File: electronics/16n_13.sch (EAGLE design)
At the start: 112 parts, among them J1 PJ302M, J10 PJ302M, J11 PJ302M, J12 PJ302M, J13 PJ302M, J14 PJ302M, J15 PJ302M, J16 PJ302M, J2 PJ302M, J3 PJ302M, J4 PJ302M, J5 PJ302M, J6 PJ302M, J7 PJ302M, J8 PJ302M, J9 PJ302M, U1 MCP6004_SMD, U2 MCP6004_SMD, U3 MCP6004_SMD, U4 MCP6004_SMD, U5 MCP6004_SMD, U6 MCP6004_SMD, U7 MCP6004_SMD, U8 MCP6004_SMD, U9 CD74HC4067SM96

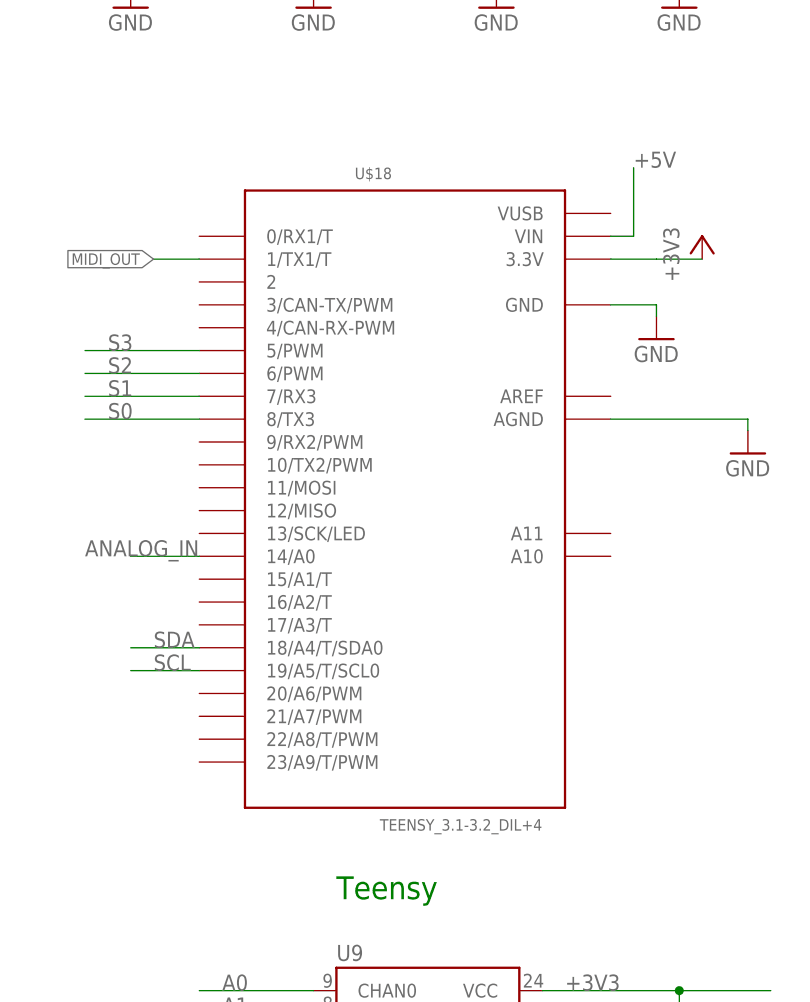
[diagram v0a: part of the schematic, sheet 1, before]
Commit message: Given Teensy 3.2 AREF is 3.3V... let's strip out the inner pins.
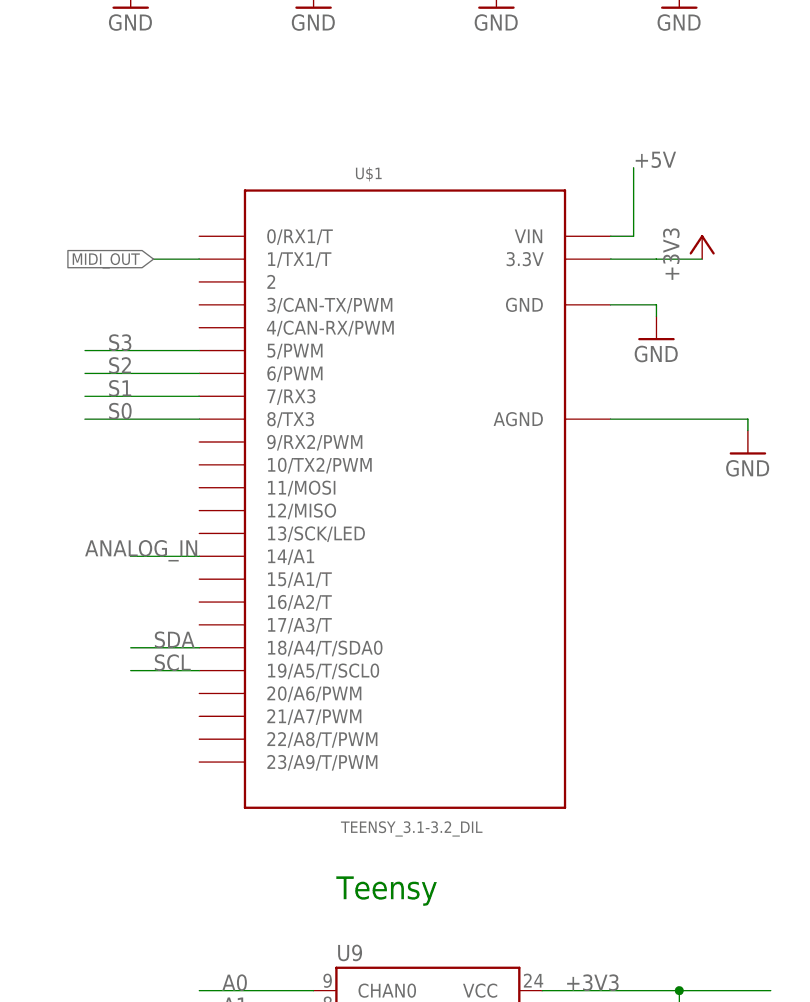
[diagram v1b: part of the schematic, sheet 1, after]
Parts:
- removed U$18: TEENSY_3.1-3.2_DIL+4, Teensy_3_and_LC_Series_Boards_v1.4:TEENSY_3.1-3.2_DIL+4
- added U$1: TEENSY_3.1-3.2_DIL, Teensy_3_and_LC_Series_Boards_v1.4:TEENSY_3.1-3.2_DIL
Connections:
- net +3V3: now also U$1.3.3V; no longer U$18.3.3V
- net +5V: now also U$1.VIN; no longer U$18.VIN
- net ANALOG_IN: now also U$1.14/A1; no longer U$18.14/A0
- net GND: now also U$1.AGND, U$1.GND; no longer U$18.AGND, U$18.GND
- net MIDI_OUT: now also U$1.1/TX1/T; no longer U$18.1/TX1/T
- net S0: now also U$1.8/TX3; no longer U$18.8/TX3
- net S1: now also U$1.7/RX3; no longer U$18.7/RX3
- net S2: now also U$1.6/PWM; no longer U$18.6/PWM
- net S3: now also U$1.5/PWM; no longer U$18.5/PWM
- net SCL: now also U$1.19/A5/T/SCL0; no longer U$18.19/A5/T/SCL0
- net SDA: now also U$1.18/A4/T/SDA0; no longer U$18.18/A4/T/SDA0
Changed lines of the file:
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@@
 <part name="GND24" library="supply1" deviceset="GND" device=""/>
 <part name="C9" library="rcl" library_urn="urn:adsk.eagle:library:334" deviceset="C-EU" device="C0805" package3d_urn="urn:adsk.eagle:package:23617/2" value="100n"/>
-<part name="U$18" library="Teensy_3_and_LC_Series_Boards_v1.4" deviceset="TEENSY_3.1-3.2_DIL+4" device=""/>
+<part name="U$1" library="Teensy_3_and_LC_Series_Boards_v1.4" deviceset="TEENSY_3.1-3.2_DIL" device=""/>
 </parts>
 <sheets>
@@
 <instance part="GND24" gate="1" x="124.46" y="12.7"/>
 <instance part="C9" gate="G$1" x="134.62" y="48.26"/>
-<instance part="U$18" gate="G$1" x="104.14" y="109.22"/>
+<instance part="U$1" gate="G$1" x="104.14" y="111.76"/>
 </instances>
 <busses>
@@
 <wire x1="127" y1="129.54" x2="132.08" y2="129.54" width="0.1524" layer="91"/>
 <wire x1="132.08" y1="129.54" x2="132.08" y2="128.27" width="0.1524" layer="91"/>
-<pinref part="U$18" gate="G$1" pin="GND"/>
+<pinref part="U$1" gate="G$1" pin="GND"/>
 </segment>
 <segment>
@@
 <wire x1="127" y1="116.84" x2="142.24" y2="116.84" width="0.1524" layer="91"/>
 <wire x1="142.24" y1="116.84" x2="142.24" y2="115.57" width="0.1524" layer="91"/>
-<pinref part="U$18" gate="G$1" pin="AGND"/>
+<pinref part="U$1" gate="G$1" pin="AGND"/>
 </segment>
 <segment>
@@
 <wire x1="127" y1="134.62" x2="132.08" y2="134.62" width="0.1524" layer="91"/>
 <wire x1="132.08" y1="134.62" x2="137.16" y2="134.62" width="0.1524" layer="91"/>
-<pinref part="U$18" gate="G$1" pin="3.3V"/>
+<pinref part="U$1" gate="G$1" pin="3.3V"/>
 </segment>
 <segment>
@@
 <wire x1="129.54" y1="137.16" x2="129.54" y2="144.78" width="0.1524" layer="91"/>
 <label x="129.54" y="144.78" size="1.778" layer="95"/>
-<pinref part="U$18" gate="G$1" pin="VIN"/>
+<pinref part="U$1" gate="G$1" pin="VIN"/>
 </segment>
 </net>
@@
 <wire x1="81.28" y1="134.62" x2="76.2" y2="134.62" width="0.1524" layer="91"/>
 <label x="76.2" y="134.62" size="1.27" layer="95" rot="R180" xref="yes"/>
-<pinref part="U$18" gate="G$1" pin="1/TX1/T"/>
+<pinref part="U$1" gate="G$1" pin="1/TX1/T"/>
 </segment>
 </net>
@@
 <wire x1="81.28" y1="91.44" x2="73.66" y2="91.44" width="0.1524" layer="91"/>
 <label x="76.2" y="91.44" size="1.778" layer="95"/>
-<pinref part="U$18" gate="G$1" pin="18/A4/T/SDA0"/>
+<pinref part="U$1" gate="G$1" pin="18/A4/T/SDA0"/>
 </segment>
 </net>
@@
 <wire x1="81.28" y1="88.9" x2="73.66" y2="88.9" width="0.1524" layer="91"/>
 <label x="76.2" y="88.9" size="1.778" layer="95"/>
-<pinref part="U$18" gate="G$1" pin="19/A5/T/SCL0"/>
+<pinref part="U$1" gate="G$1" pin="19/A5/T/SCL0"/>
 </segment>
 </net>
@@
 <wire x1="81.28" y1="101.6" x2="73.66" y2="101.6" width="0.1524" layer="91"/>
 <label x="68.58" y="101.6" size="1.778" layer="95"/>
-<pinref part="U$18" gate="G$1" pin="14/A0"/>
+<pinref part="U$1" gate="G$1" pin="14/A1"/>
 </segment>
 <segment>
@@
 <wire x1="81.28" y1="116.84" x2="68.58" y2="116.84" width="0.1524" layer="91"/>
 <label x="71.12" y="116.84" size="1.778" layer="95"/>
-<pinref part="U$18" gate="G$1" pin="8/TX3"/>
+<pinref part="U$1" gate="G$1" pin="8/TX3"/>
 </segment>
 <segment>
@@
 <wire x1="81.28" y1="119.38" x2="68.58" y2="119.38" width="0.1524" layer="91"/>
 <label x="71.12" y="119.38" size="1.778" layer="95"/>
-<pinref part="U$18" gate="G$1" pin="7/RX3"/>
+<pinref part="U$1" gate="G$1" pin="7/RX3"/>
 </segment>
 <segment>
@@
 <wire x1="81.28" y1="121.92" x2="68.58" y2="121.92" width="0.1524" layer="91"/>
 <label x="71.12" y="121.92" size="1.778" layer="95"/>
-<pinref part="U$18" gate="G$1" pin="6/PWM"/>
+<pinref part="U$1" gate="G$1" pin="6/PWM"/>
 </segment>
 <segment>
@@
 <wire x1="81.28" y1="124.46" x2="68.58" y2="124.46" width="0.1524" layer="91"/>
 <label x="71.12" y="124.46" size="1.778" layer="95"/>
-<pinref part="U$18" gate="G$1" pin="5/PWM"/>
-</segment>
-<segment>
+<pinref part="U$1" gate="G$1" pin="5/PWM"/>
+</segment>
+<segment>

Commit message: Tidying and eyeballing layout.
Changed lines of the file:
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@@
 <pinref part="U9" gate="U1" pin="COM"/>
 <wire x1="119.38" y1="25.4" x2="132.08" y2="25.4" width="0.1524" layer="91"/>
+<label x="132.08" y="25.4" size="1.778" layer="95"/>
 </segment>
 </net>
@@
 <segment>
 <pinref part="U9" gate="U1" pin="CHAN15"/>
-<wire x1="93.98" y1="15.24" x2="86.36" y2="15.24" width="0.1524" layer="91"/>
-<label x="88.9" y="15.24" size="1.778" layer="95"/>
+<wire x1="93.98" y1="15.24" x2="81.28" y2="15.24" width="0.1524" layer="91"/>
+<label x="83.82" y="15.24" size="1.778" layer="95"/>
 </segment>
 </net>
